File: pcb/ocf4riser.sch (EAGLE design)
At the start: 38 parts, among them IC1 STM32F405RGTx, IC2 MCP1703CB, IC3 W25Q80BV, IC4 TPD3E001DRL, IC5 STMPS2141STR, J1 TEENSY_3.1-3.2_DIL, J2 CORTEX_DEBUGNAKED, X1 TXC-7A

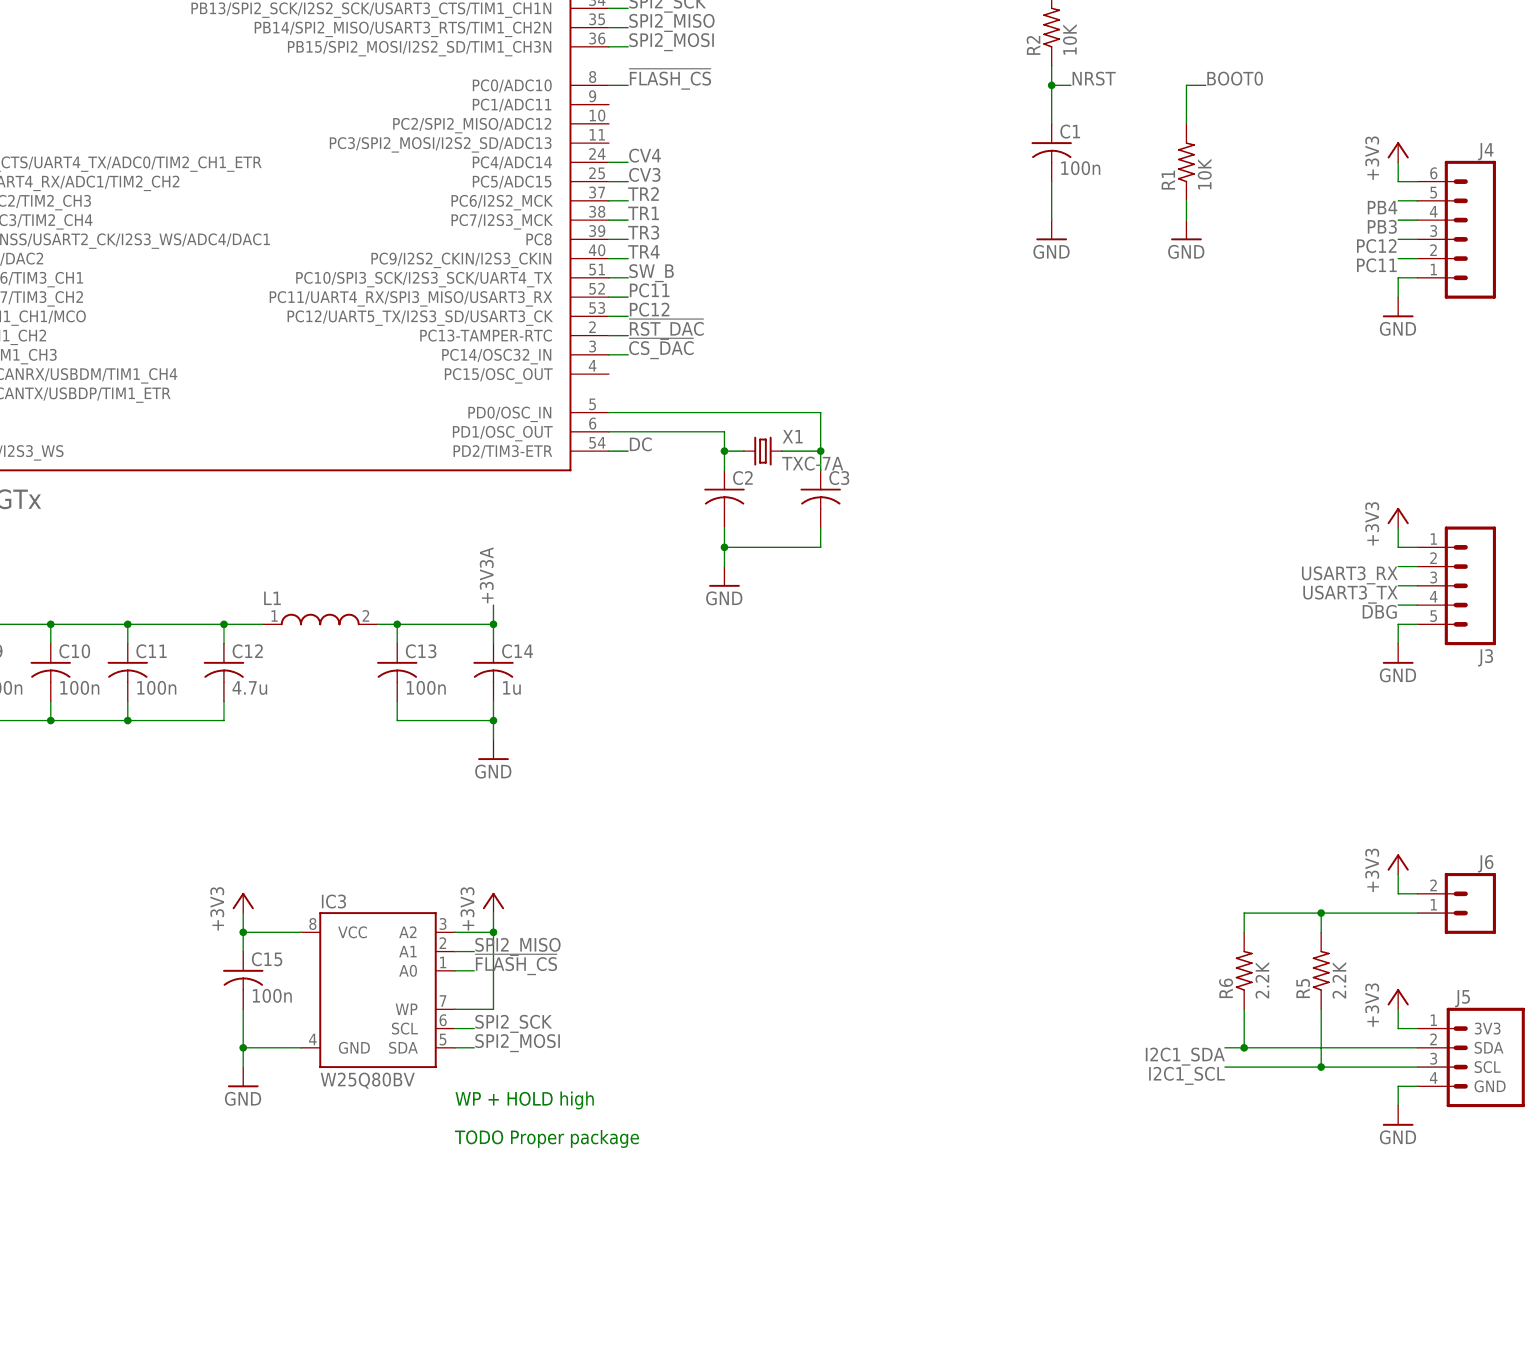
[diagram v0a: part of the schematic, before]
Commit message: Pin headers, values & names
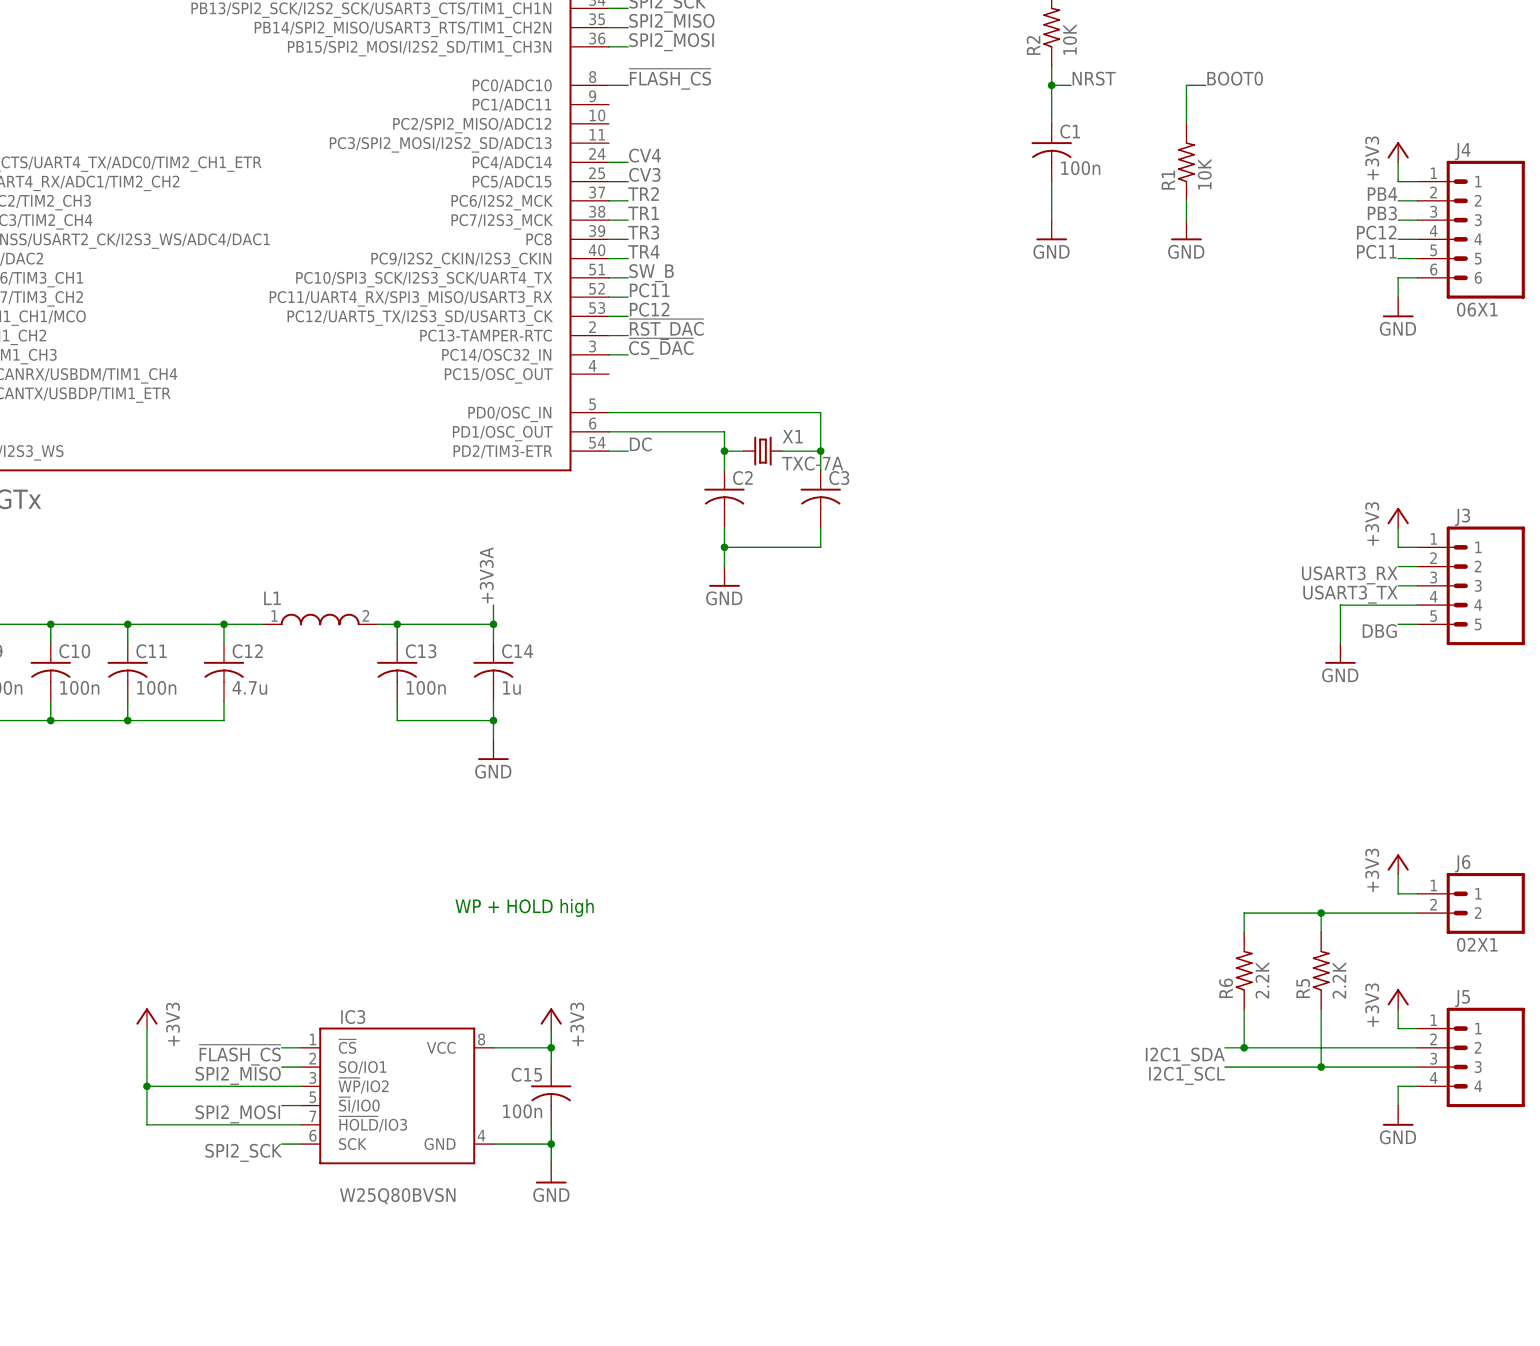
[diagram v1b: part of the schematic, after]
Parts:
- IC3: value W25Q80BV -> W25Q80BVSN; device pld-eeprom:24XX512SN -> pld-eeprom:SPIFLASHN
- J3: device SparkFun-Connectors:M05PTH -> pld-headers:05X1
- J4: value (none) -> 06X1; device SparkFun-Connectors:M06SILK_FEMALE_PTH -> pld-headers:06X1
- J5: device pld-misc:I2C -> pld-headers:04X1
- J6: value (none) -> 02X1; device SparkFun-Connectors:M02PTH -> pld-headers:02X1
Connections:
- net !FLASH_CS: now also IC3.!CS!; no longer IC3.A0
- net +3V3: now also IC3.!HOLD!/IO3, IC3.!WP!/IO2, J4.1, J5.1, J6.1; no longer IC3.A2, IC3.WP, J4.6, J5.3V3, J6.2
- net DBG: now also J3.5; no longer J3.4
- net GND: now also J3.4, J4.6, J5.4; no longer J3.5, J4.1, J5.GND
- net I2C1_SCL: now also J5.3; no longer J5.SCL
- net I2C1_SDA: now also J5.2; no longer J5.SDA
- net I2C_PU: now also J6.2; no longer J6.1
- net PB3: now also J4.3; no longer J4.4
- net PB4: now also J4.2; no longer J4.5
- net PC11: now also J4.5; no longer J4.2
- net PC12: now also J4.4; no longer J4.3
- net SPI2_MISO: now also IC3.SO/IO1; no longer IC3.A1
- net SPI2_MOSI: now also IC3.!SI!/IO0; no longer IC3.SDA
- net SPI2_SCK: now also IC3.SCK; no longer IC3.SCL
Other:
- note removed: "TODO Proper package"
- moved on the sheet: C15, IC3

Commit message: Tweaks
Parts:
- added C17: 22u, pld-rcl:C-USC0805
- added L2: R/L, SparkFun-Passives:INDUCTOR0805
- added R9: 47k, pld-rcl:R-US_R0402
- C16: value 4.7u -> 2.2u
- C2, C3: value (none) -> 33p
- J2: value CORTEX_DEBUGNAKED -> SWD/JTAG
- J3: value (none) -> DEBUG
- J4: value 06X1 -> IO
- J5: value (none) -> I2C
- USB: value MOLEX-105133 -> (none); device pld-usb-con:MOLEX-105133 -> pld-usb-con:614105150621
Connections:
- removed net !USB_FAULT: IC5.!FAULT
- new net !USB_PWR_FAULT: IC1.PB1/ADC9/TIM3_CH4, IC5.!FAULT, R9.1
- new net N$1: C17.1, J1.3.3V, L2.1
- net +3V3: now also L2.2, R9.2; no longer J1.3.3V
- net ENC_L1: now also IC1.PB2/BOOT1; no longer IC1.PB1/ADC9/TIM3_CH4
- net GND: now also C17.2, USB.5GND, USB.GND@1, USB.GND@2; no longer USB.GND, USB.S
- net N$4: now also USB.2D-; no longer USB.D-
- net N$7: now also USB.3D+; no longer USB.D+
- net USB_ID: now also USB.4ID; no longer USB.ID
- net USB_VBUS: now also USB.1VCC; no longer USB.VCC
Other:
- note added: "Crystal Cl=18p C = 2x(Cl - Cp) = 2x(18-{3-5}) = 30-26p"
- note added: "OTG power"
- note added: "PB2 = BOOT1 0 = system, 1 = SRAM"
- note removed: "PB2 = BOOT1"
- moved on the sheet: C16, IC4, IC5, R3, R4, R7, R8

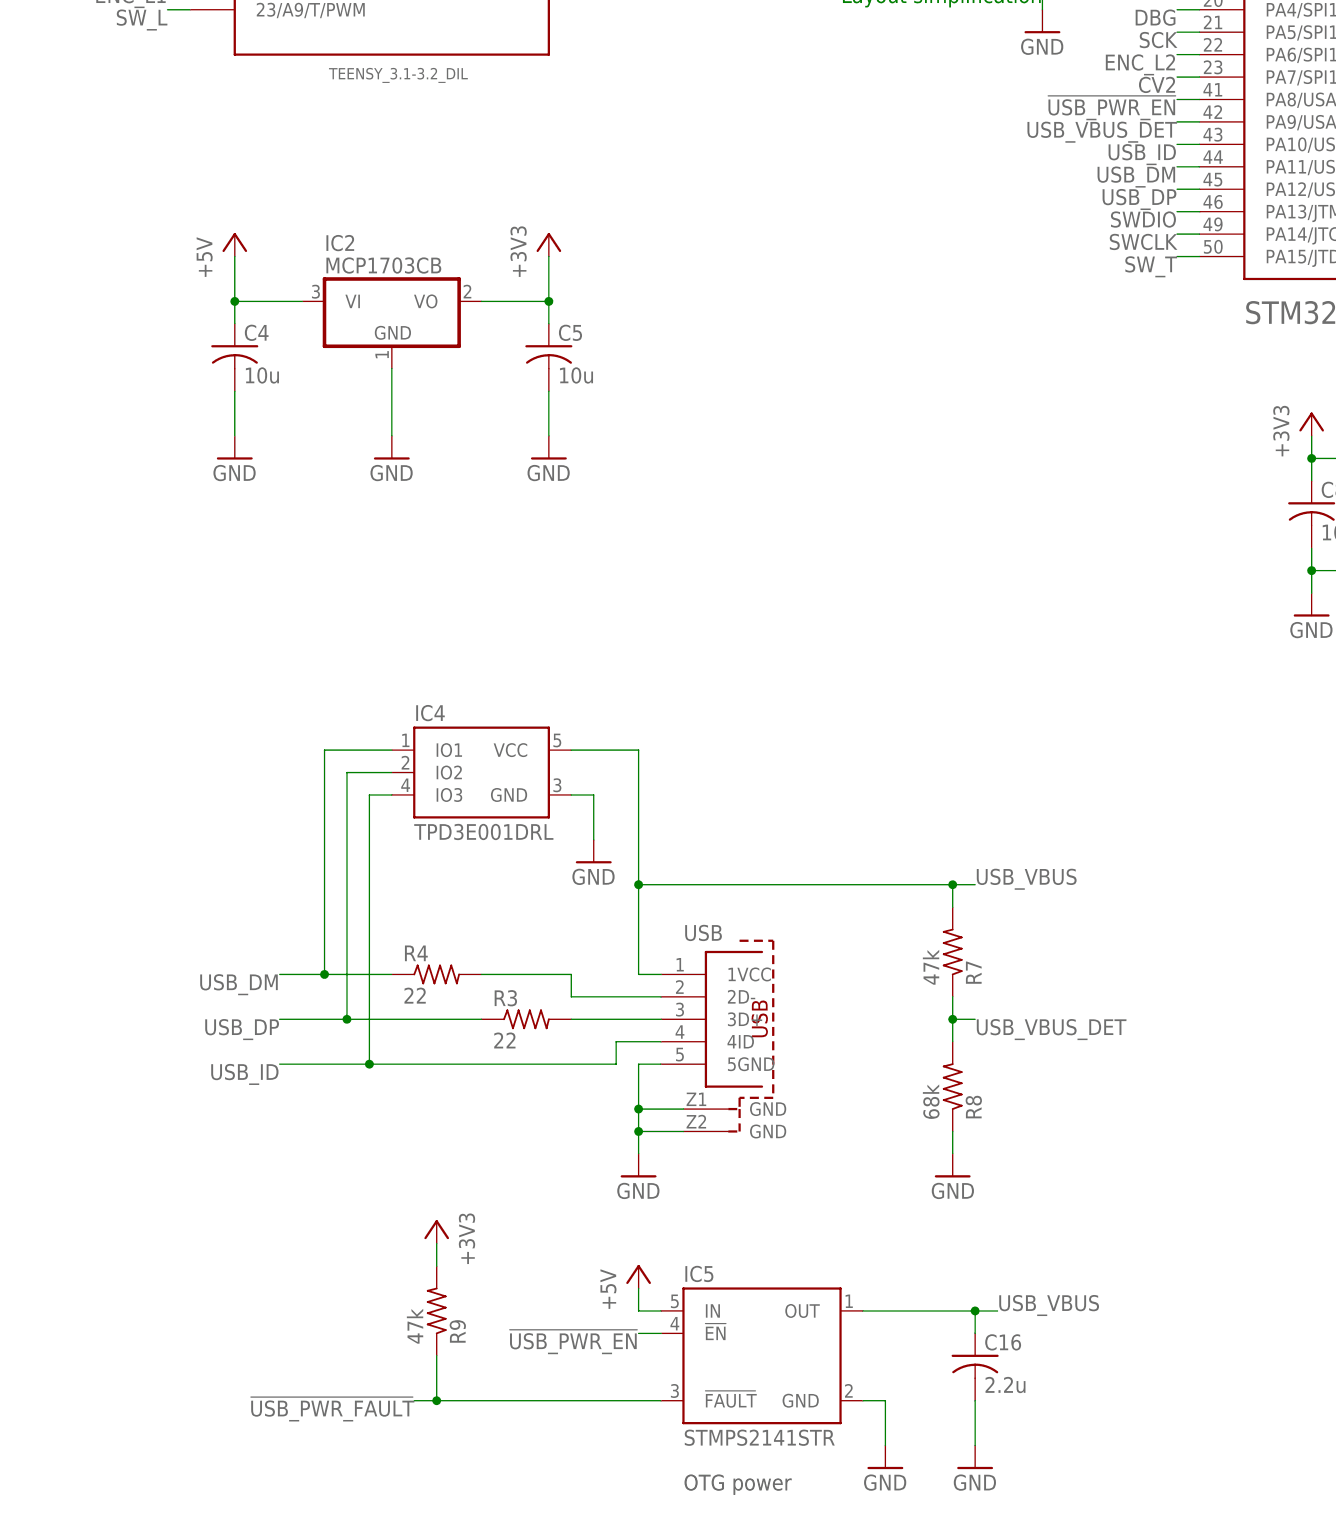
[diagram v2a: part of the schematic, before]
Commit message: USB as header instead of receptacle
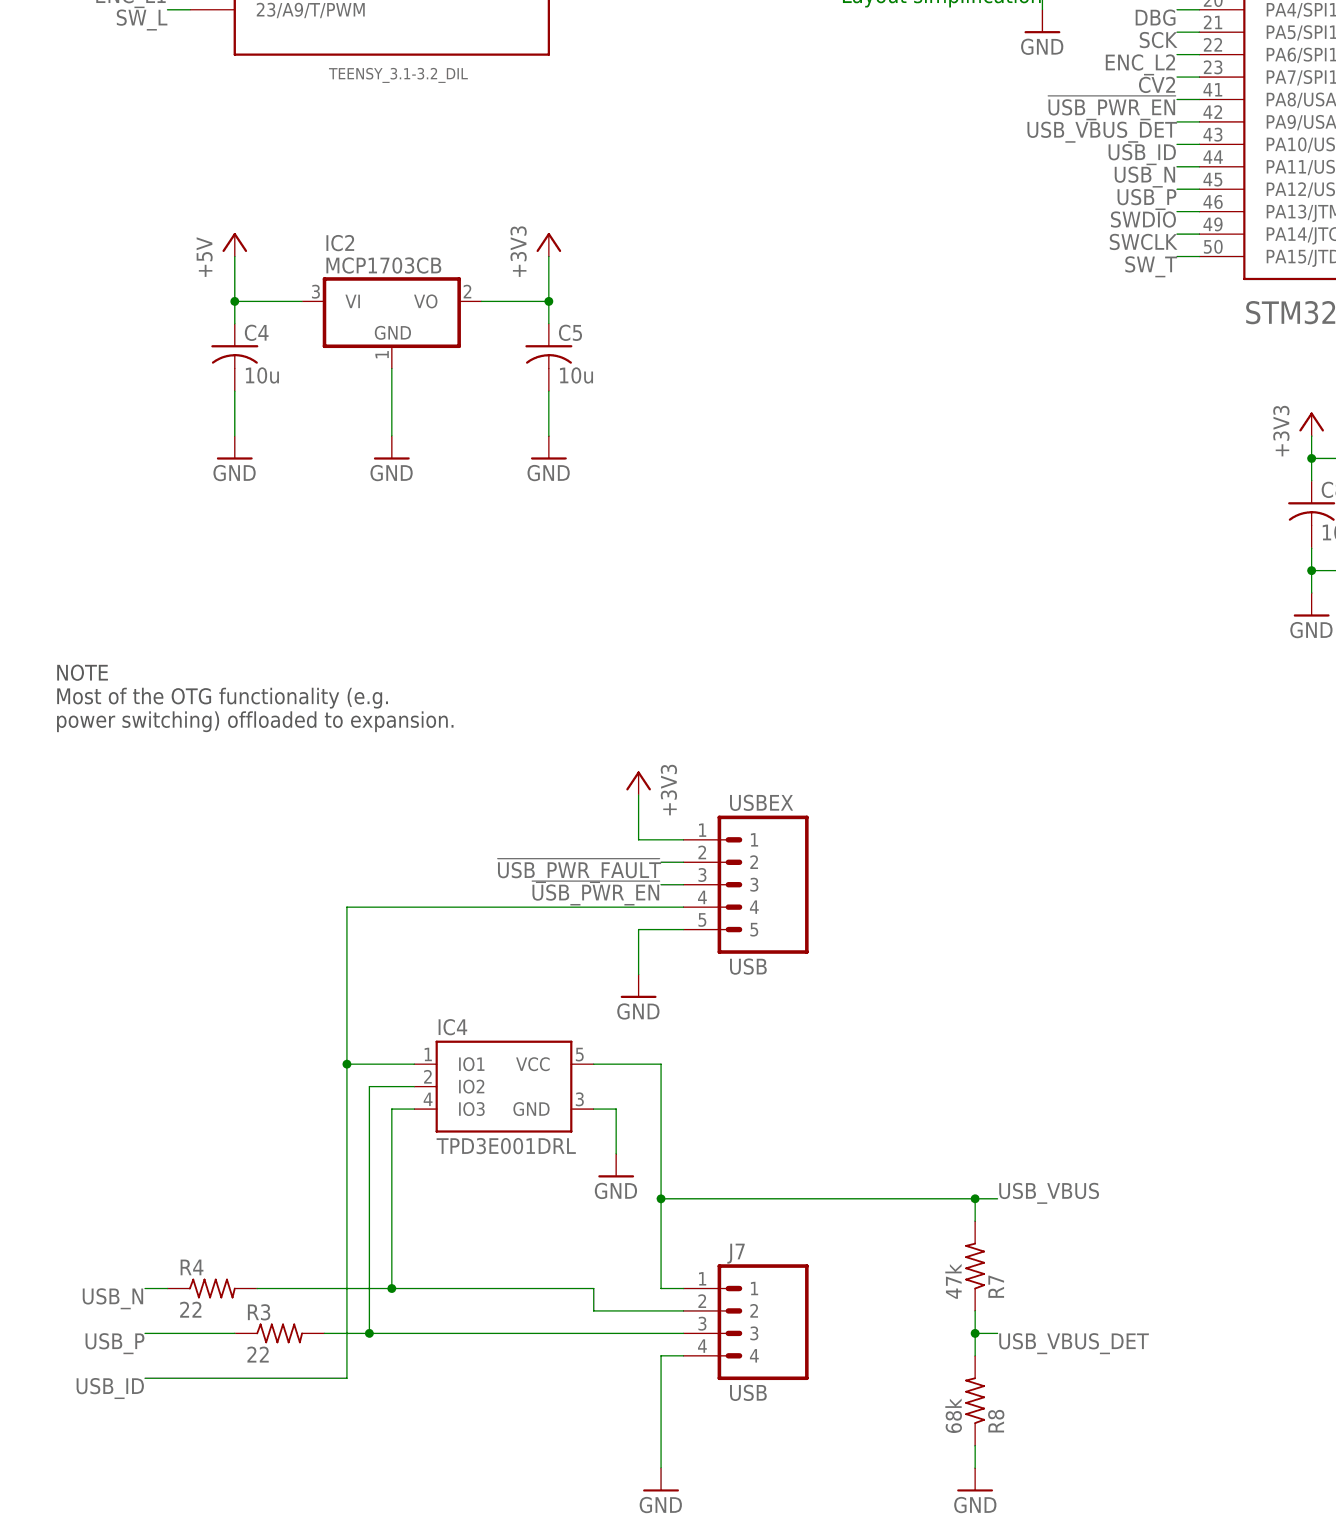
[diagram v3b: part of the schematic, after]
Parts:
- removed C16: 2.2u, pld-rcl:C-USC0603
- removed IC5: STMPS2141STR, pld-usb-st:STMPS2141STR
- removed R9: 47k, pld-rcl:R-US_R0402
- removed USB: (no value), pld-usb-con:614105150621
- added J7: USB, pld-headers:04X1
- added USBEX: USB, pld-headers:05X1
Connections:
- removed net N$4: R4.2, USB.2D-
- removed net N$7: R3.2, USB.3D+
- removed net USB_DM: IC1.PA11/USART1_CTS/CANRX/USBDM/TIM1_CH4, IC4.IO1, R4.1
- removed net USB_DP: IC1.PA12/USART1_RTS/CANTX/USBDP/TIM1_ETR, IC4.IO2, R3.1
- new net USB_I_N: IC4.IO3, J7.2, R4.2
- new net USB_I_P: IC4.IO2, J7.3, R3.2
- new net USB_N: IC1.PA11/USART1_CTS/CANRX/USBDM/TIM1_CH4, R4.1
- new net USB_P: IC1.PA12/USART1_RTS/CANTX/USBDP/TIM1_ETR, R3.1
- net !USB_PWR_EN: now also USBEX.3; no longer IC5.!EN
- net !USB_PWR_FAULT: now also USBEX.2; no longer IC5.!FAULT, R9.1
- net +3V3: now also USBEX.1; no longer R9.2
- net +5V: no longer IC5.IN
- net GND: now also J7.4, USBEX.5; no longer C16.2, IC5.GND, USB.5GND, USB.GND@1, USB.GND@2
- net USB_ID: now also IC4.IO1, USBEX.4; no longer IC4.IO3, USB.4ID
- net USB_VBUS: now also J7.1; no longer C16.1, IC5.OUT, USB.1VCC
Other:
- note added: "NOTE Most of the OTG functionality (e.g. power switching) offloaded to expansion."
- note removed: "OTG power"
- moved on the sheet: IC4, R3, R4, R7, R8
